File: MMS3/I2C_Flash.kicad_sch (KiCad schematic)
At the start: 9 parts, among them U6 AT24C256C

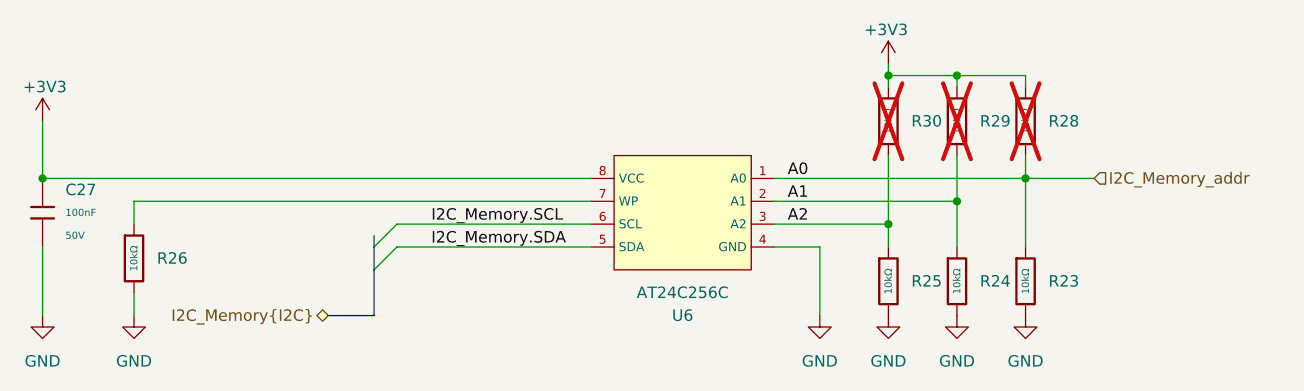
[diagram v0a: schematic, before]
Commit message: schematic + partly layout
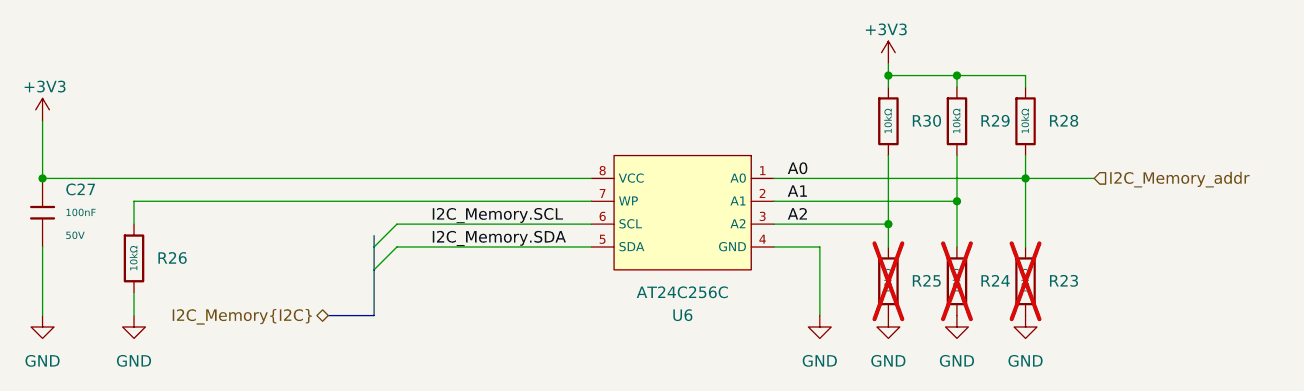
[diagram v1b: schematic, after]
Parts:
- R23, R24, R25: now not fitted; now left out of the parts list
- R28, R29, R30: now fitted; now in the parts list
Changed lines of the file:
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@@
 		(body_style 1)
 		(exclude_from_sim no)
-		(in_bom no)
+		(in_bom yes)
 		(on_board yes)
 		(in_pos_files yes)
-		(dnp yes)
+		(dnp no)
 		(fields_autoplaced yes)
 		(property "Reference" "R30"
@@
 		(body_style 1)
 		(exclude_from_sim no)
-		(in_bom no)
+		(in_bom yes)
 		(on_board yes)
 		(in_pos_files yes)
-		(dnp yes)
+		(dnp no)
 		(fields_autoplaced yes)
 		(property "Reference" "R28"
@@
 		(body_style 1)
 		(exclude_from_sim no)
-		(in_bom yes)
+		(in_bom no)
 		(on_board yes)
 		(in_pos_files yes)
-		(dnp no)
+		(dnp yes)
 		(fields_autoplaced yes)
 		(property "Reference" "R23"
@@
 		(body_style 1)
 		(exclude_from_sim no)
-		(in_bom no)
+		(in_bom yes)
 		(on_board yes)
 		(in_pos_files yes)
-		(dnp yes)
+		(dnp no)
 		(fields_autoplaced yes)
 		(property "Reference" "R29"
@@
 		(body_style 1)
 		(exclude_from_sim no)
-		(in_bom yes)
+		(in_bom no)
 		(on_board yes)
 		(in_pos_files yes)
-		(dnp no)
+		(dnp yes)
 		(fields_autoplaced yes)
 		(property "Reference" "R24"
@@
 		(body_style 1)
 		(exclude_from_sim no)
-		(in_bom yes)
+		(in_bom no)
 		(on_board yes)
 		(in_pos_files yes)
-		(dnp no)
+		(dnp yes)
 		(fields_autoplaced yes)
 		(property "Reference" "R25"
